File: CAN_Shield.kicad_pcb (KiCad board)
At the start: 2 copper layers, 65 x 56 mm, 5 parts, among them J1 GPIO

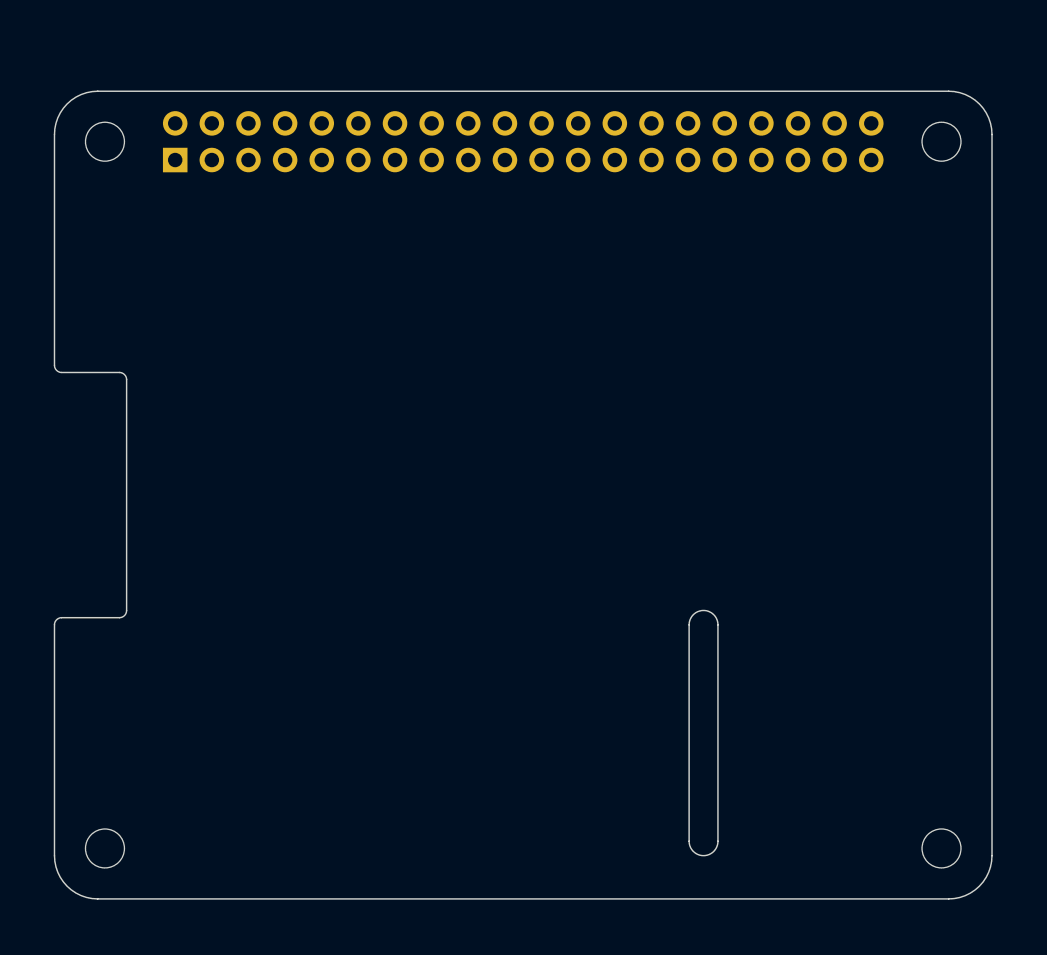
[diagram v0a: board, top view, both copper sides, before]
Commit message: finished layout with 9 pin screw terminal, Unfinished edge extend and diff pair CAN
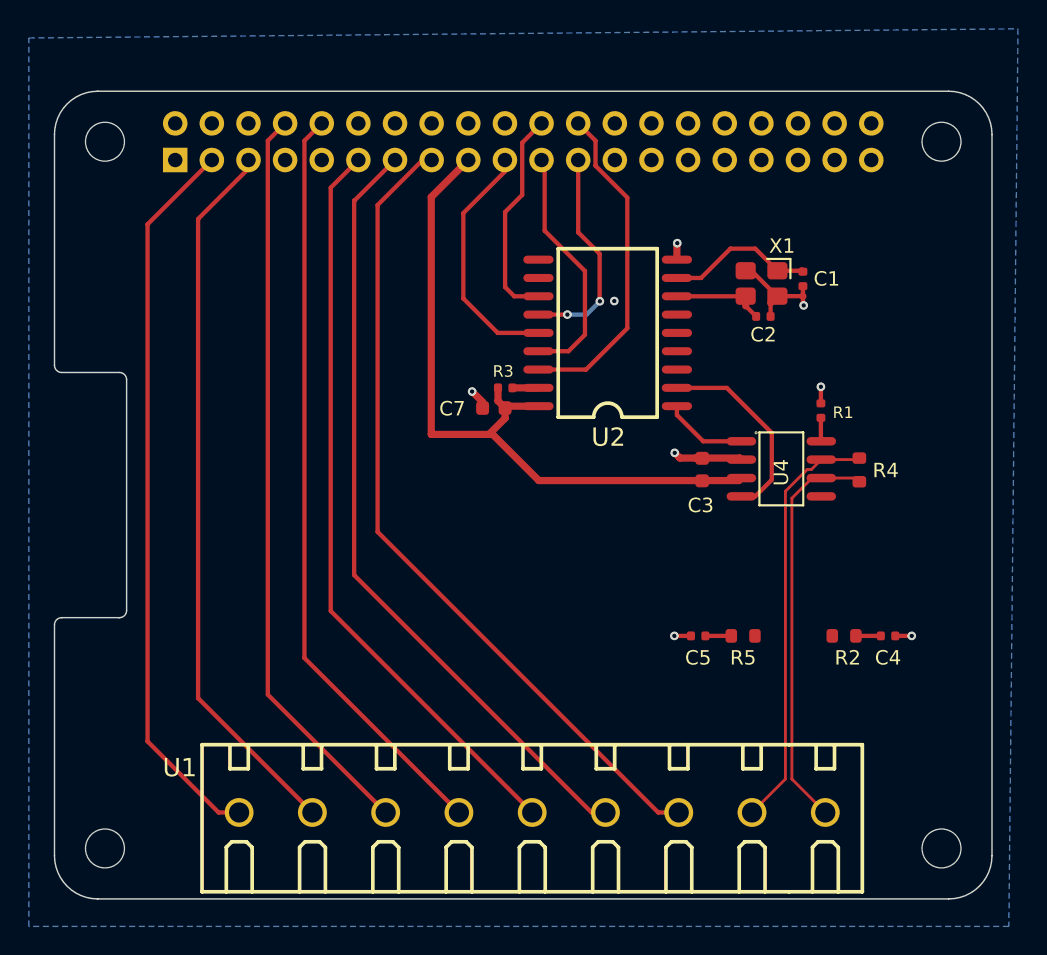
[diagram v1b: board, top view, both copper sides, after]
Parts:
- added C1: 22pF, PCM_JLCPCB:C_0402, F.Cu at (151.9, 57.0)
- added C2: 22pF, PCM_JLCPCB:C_0402, F.Cu at (149.1, 59.6)
- added C3: 100nF, PCM_JLCPCB:C_0603, F.Cu at (144.9, 70.2)
- added C4: 470pF, PCM_JLCPCB:C_0402, F.Cu at (157.8, 81.8)
- added C5: 470pF, PCM_JLCPCB:C_0402, F.Cu at (144.6, 81.8)
- added C7: 100nF, PCM_JLCPCB:C_0603, F.Cu at (130.5, 66.0)
- added R1: 4.7kΩ, PCM_JLCPCB:R_0402, F.Cu at (153.1, 66.1)
- added R2: 120Ω, PCM_JLCPCB:R_0603, F.Cu at (154.7, 81.8)
- added R3: 4.7kΩ, PCM_JLCPCB:R_0402, F.Cu at (131.2, 64.6)
- added R4: 120Ω, PCM_JLCPCB:R_0603, F.Cu at (155.8, 70.3)
- added R5: 120Ω, PCM_JLCPCB:R_0603, F.Cu at (147.7, 81.8)
- added U1: MX128-5.08-09P-GN01-CU-Y-A, ImportFP:CONN-TH_9P-P5.08_MX128-5.08-09P-GN01-CU-Y-A, F.Cu at (133.1, 94.0)
- added U2: MCP2515T-I/SO, ImportFP:MCP2515T-IST_SOIC-18_L11.6-W7.5-P1.27-LS10.3-BL, F.Cu at (138.4, 60.8)
- added U4: SN65HVD230DR, PCM_JLCPCB:SOIC-8_L4.9-W3.9-P1.27-LS6.0-BL, F.Cu at (150.4, 70.2)
- added X1: X322516MLB4SI, PCM_JLCPCB:OSC-SMD_4P-L3.2-W2.5-BL, F.Cu at (149.0, 57.3)
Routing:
- net /GPIO22: track 0.00 -> 56.6 mm
- net /GPIO27: track 0.00 -> 54.2 mm
- net /GPIO15/RXD0: track 0.00 -> 52.7 mm
- net /GPIO17: track 0.00 -> 51.8 mm
- net /GPIO14/TXD0: track 0.00 -> 51.7 mm
- net /GPIO2/SDA1: track 0.00 -> 50.5 mm
- net /GPIO3/SCL1: track 0.00 -> 50.0 mm
- net +3V3: track 0.00 -> 49.2 mm
- net /CAN_D+: track 0.00 -> 29.3 mm
- net /CAN_D-: track 0.00 -> 28.1 mm
- net /GPIO8/SPI0.CE0: track 0.00 -> 23.0 mm
- net GND: track 0.00 -> 19.3 mm, vias 0 -> 8
- net /GPIO9/SPI0.MISO: track 0.00 -> 17.1 mm
- net /GPIO10/SPI0.MOSI: track 0.00 -> 17.0 mm
- net /GPIO11/SPI0.SCLK: track 0.00 -> 15.1 mm, vias 0 -> 2
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- added copper zone on B.Cu, net GND
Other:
- outline, holes or cut-outs redrawn
- board text removed: "CAMERA (OPTIONAL)"

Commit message: change from gpio to gnd at screw terminal and add copper pour for gnd
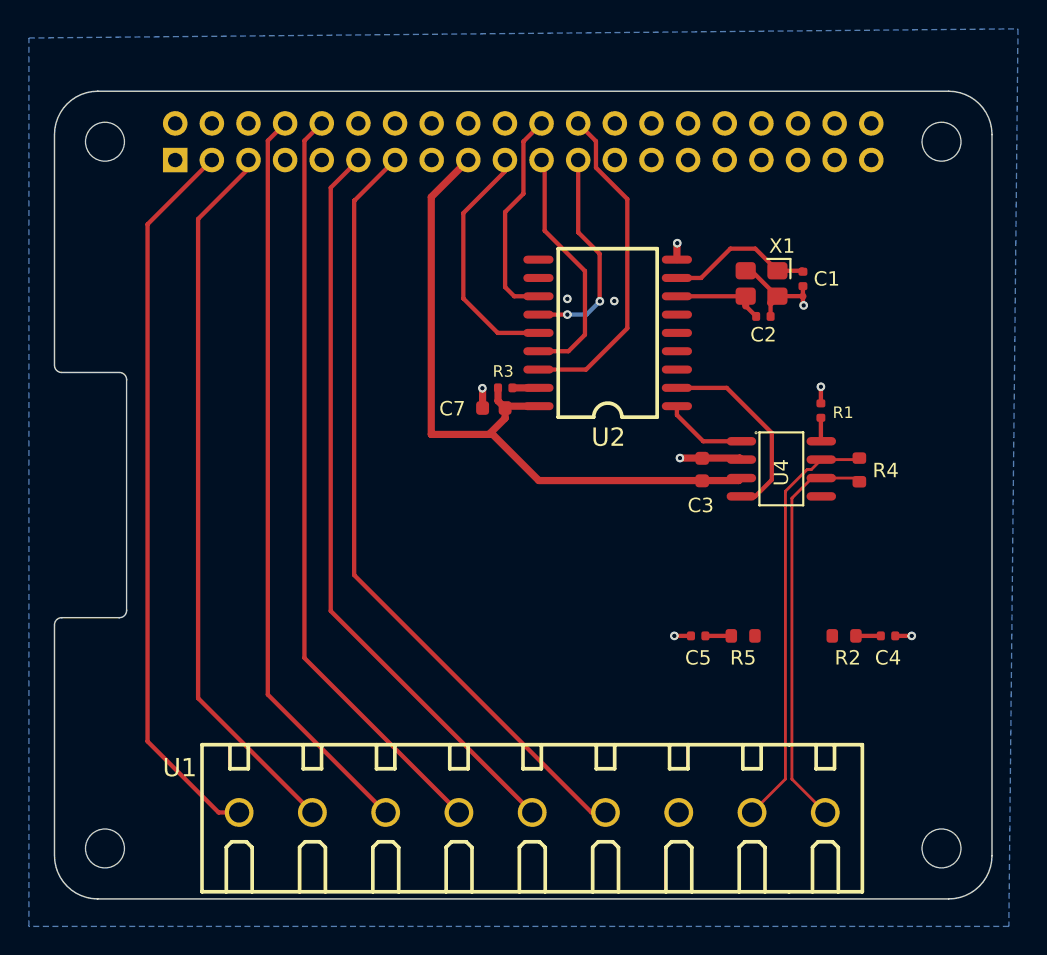
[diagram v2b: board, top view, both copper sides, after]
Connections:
- U1 pad 7: /GPIO22 -> GND
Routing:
- net /GPIO22: track 56.6 -> 0.62 mm
- net GND: track 19.3 -> 18.7 mm, vias 8 -> 9
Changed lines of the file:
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@@
 			)
 			(remove_unused_layers no)
-			(net 10 "/GPIO22")
+			(net 1 "GND")
 			(pinfunction "7")
 			(pintype "unspecified")
@@
 			(net 10 "/GPIO22")
 			(pinfunction "Pin_15")
-			(pintype "passive")
+			(pintype "passive+no_connect")
 		)
 		(pad "16" thru_hole oval
@@
 	)
 	(segment
-		(start 147.5164 69.4332)
-		(end 147.6236 69.5404)
-		(width 0.5)
-		(layer "F.Cu")
-		(net 1)
-	)
-	(segment
 		(start 149.649 59.614)
 		(end 149.649 58.681)
@@
 	)
 	(segment
+		(start 147.5164 69.4332)
+		(end 147.6236 69.5404)
+		(width 0.5)
+		(layer "F.Cu")
+		(net 1)
+	)
+	(segment
 		(start 148.325122 56.448)
 		(end 150.085122 58.208)
@@
 	)
 	(segment
-		(start 144.45 69.4332)
-		(end 147.5164 69.4332)
-		(width 0.5)
-		(layer "F.Cu")
-		(net 1)
-	)
-	(segment
 		(start 158.293 81.7628)
 		(end 159.436 81.7628)
@@
 	)
 	(segment
-		(start 129.682 65.964)
-		(end 129.682 65.547)
+		(start 149.649 58.681)
+		(end 150.122 58.208)
 		(width 0.5)
 		(layer "F.Cu")
@@
 	)
 	(segment
-		(start 149.649 58.681)
-		(end 150.122 58.208)
+		(start 151.891 58.8)
+		(end 151.943 58.852)
 		(width 0.5)
 		(layer "F.Cu")
@@
 	)
 	(segment
-		(start 151.891 58.8)
-		(end 151.943 58.852)
+		(start 129.682 64.6072)
+		(end 129.682 65.964)
 		(width 0.5)
 		(layer "F.Cu")
@@
 	)
 	(segment
-		(start 129.682 65.547)
-		(end 128.956 64.821)
+		(start 143.3652 69.4332)
+		(end 147.5164 69.4332)
 		(width 0.5)
 		(layer "F.Cu")
@@
 	)
 	(segment
-		(start 143.3652 69.4332)
-		(end 143.0022 69.0702)
+		(start 129.6672 64.5924)
+		(end 129.682 64.6072)
 		(width 0.5)
 		(layer "F.Cu")
@@
 	)
 	(segment
-		(start 144.45 69.4332)
-		(end 143.3652 69.4332)
-		(width 0.5)
-		(layer "F.Cu")
-		(net 1)
-	)
-	(segment
 		(start 143.1541 54.5599)
 		(end 143.18 54.534)
@@
 	)
 	(via
+		(at 135.56 58.3948)
+		(size 0.6)
+		(drill 0.3)
+		(layers "F.Cu" "B.Cu")
+		(net 1)
+	)
+	(via
 		(at 142.9768 81.7628)
 		(size 0.6)
@@
 	)
 	(via
-		(at 128.956 64.821)
+		(at 129.6672 64.5924)
 		(size 0.6)
 		(drill 0.3)
@@
 	)
 	(via
-		(at 143.0022 69.0702)
+		(at 143.3652 69.4332)
 		(size 0.6)
 		(drill 0.3)
@@
 	)
 	(segment
-		(start 122.4028 74.5492)
-		(end 141.8592 94.0056)
-		(width 0.3)
-		(layer "F.Cu")
-		(net 10)
-	)
-	(segment
-		(start 125.5252 48.77)
-		(end 122.4028 51.8924)
-		(width 0.3)
-		(layer "F.Cu")
-		(net 10)
-	)
-	(segment
 		(start 126.15 48.77)
 		(end 125.5252 48.77)
@@
 	)
 	(segment
-		(start 122.4028 51.8924)
-		(end 122.4028 74.5492)
-		(width 0.3)
-		(layer "F.Cu")
-		(net 10)
-	)
-	(segment
-		(start 141.8592 94.0056)
-		(end 143.2816 94.0056)
-		(width 0.3)
-		(layer "F.Cu")
-		(net 10)
-	)
-	(segment
 		(start 128.3464 52.4512)
 		(end 128.3464 58.3694)
@@
 	)
 	(segment
-		(start 131.242 57.582)
-		(end 131.877 58.217)
+		(start 131.877 58.217)
+		(end 133.5539 58.217)
 		(width 0.3)
 		(layer "F.Cu")
@@
 	)
 	(segment
-		(start 131.242 52.375)
-		(end 131.242 57.582)
+		(start 132.512 51.105)
+		(end 131.242 52.375)
 		(width 0.3)
 		(layer "F.Cu")
@@
 	)
 	(segment
-		(start 132.43 47.57)
-		(end 132.43 51.187)
+		(start 131.242 57.582)
+		(end 131.877 58.217)
 		(width 0.3)
 		(layer "F.Cu")
@@
 	)
 	(segment
-		(start 133.77 46.23)
-		(end 132.43 47.57)
+		(start 132.512 47.488)
+		(end 132.512 51.105)
 		(width 0.3)
 		(layer "F.Cu")
@@
 	)
 	(segment
-		(start 131.877 58.217)
-		(end 133.5539 58.217)
+		(start 131.242 52.375)
+		(end 131.242 57.582)
 		(width 0.3)
 		(layer "F.Cu")
@@
 	)
 	(segment
-		(start 132.43 51.187)
-		(end 131.242 52.375)
+		(start 133.77 46.23)
+		(end 132.512 47.488)
 		(width 0.3)
 		(layer "F.Cu")
@@
 	)
 	(segment
-		(start 136.8554 63.297)
-		(end 133.5539 63.297)
+		(start 137.5412 47.4612)
+		(end 137.5412 49.3016)
 		(width 0.3)
 		(layer "F.Cu")
@@
 	)
 	(segment
-		(start 137.51 47.43)
-		(end 137.51 49.1688)
+		(start 139.7152 51.4756)
+		(end 139.7152 60.4372)
 		(width 0.3)
 		(layer "F.Cu")
@@
 	)
 	(segment
-		(start 137.51 49.1688)
-		(end 139.7152 51.374)
+		(start 136.8554 63.297)
+		(end 133.5539 63.297)
 		(width 0.3)
 		(layer "F.Cu")
@@
 	)
 	(segment
-		(start 139.7152 51.374)
-		(end 139.7152 60.4372)
+		(start 137.5412 49.3016)
+		(end 139.7152 51.4756)
 		(width 0.3)
 		(layer "F.Cu")
@@
 	(segment
 		(start 136.31 46.23)
-		(end 137.51 47.43)
+		(end 137.5412 47.4612)
 		(width 0.3)
 		(layer "F.Cu")

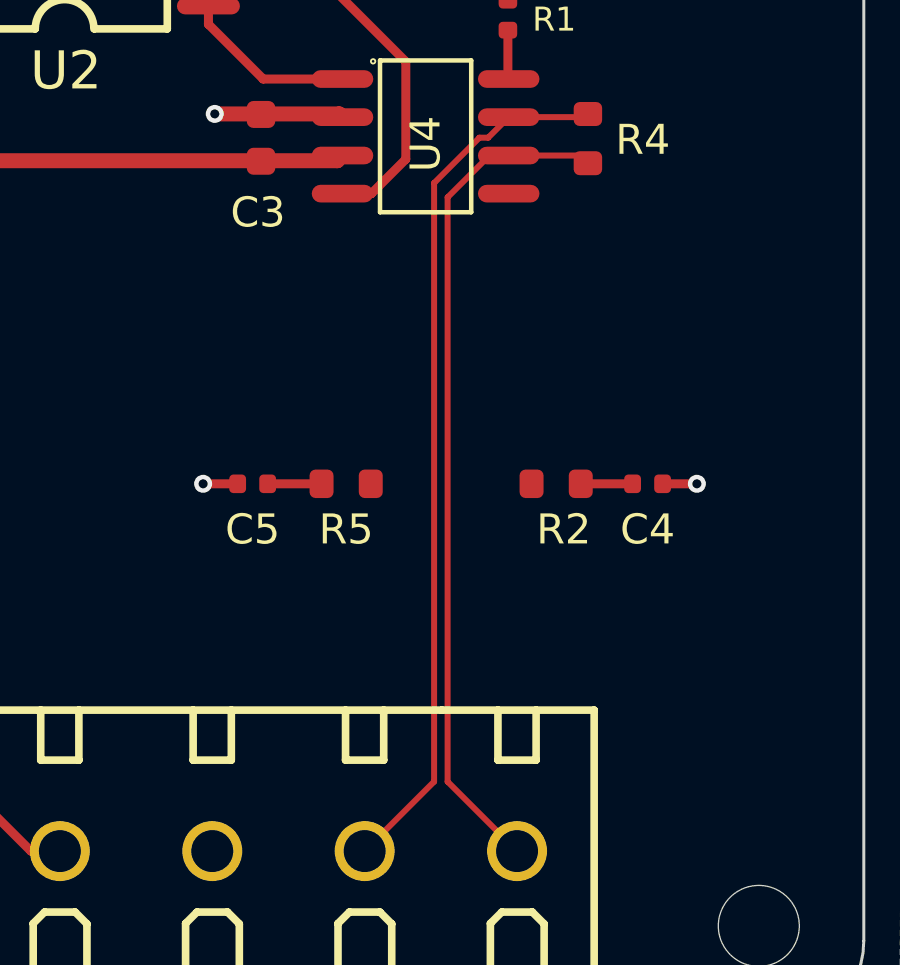
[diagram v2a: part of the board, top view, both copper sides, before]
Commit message: add R and C to CAN H,L diff pair
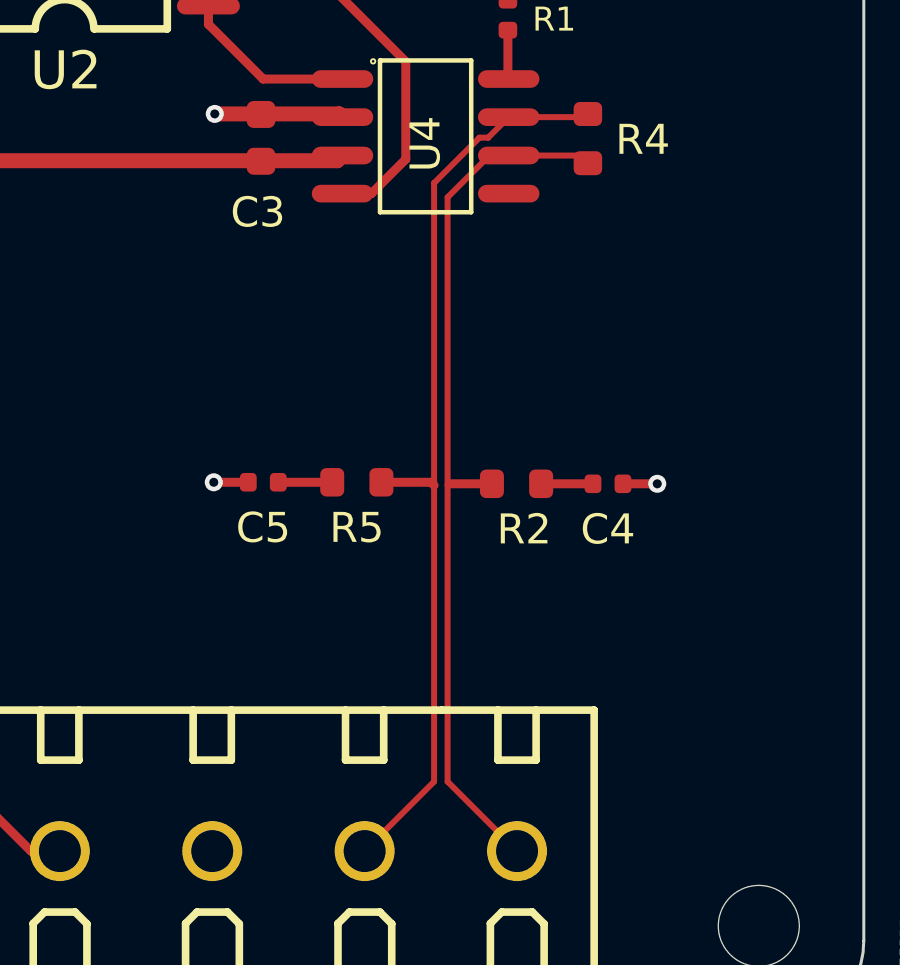
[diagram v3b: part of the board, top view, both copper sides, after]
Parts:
- moved C4 1.32 mm to (156.5, 81.8)
- moved R2 1.32 mm to (153.4, 81.8)
- moved R5 0.36 mm to (148.1, 81.7)
- moved C5 0.36 mm to (145.0, 81.7)
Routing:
- net /CAN_D+: track 29.3 -> 31.1 mm
- net /CAN_D-: track 28.1 -> 29.5 mm
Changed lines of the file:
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@@
 	(footprint "PCM_JLCPCB:C_0402"
 		(layer "F.Cu")
-		(at 144.6278 81.7628 180)
+		(at 144.9834 81.712 180)
 		(descr "Capacitor SMD 0402 (1005 Metric), square (rectangular) end terminal, IPC_7351 nominal, (Body size source: IPC-SM-782 page 76, https://www.pcb-3d.com/wordpress/wp-content/uploads/ipc-sm-782a_amendment_1_and_2.pdf), generated with kicad-footprint-generator")
 		(tags "capacitor")
@@
 	(footprint "PCM_JLCPCB:R_0603"
 		(layer "F.Cu")
-		(at 147.7448 81.7628 180)
+		(at 148.1004 81.712 180)
 		(descr "Resistor SMD 0603 (1608 Metric), square (rectangular) end terminal, IPC_7351 nominal, (Body size source: IPC-SM-782 page 72, https://www.pcb-3d.com/wordpress/wp-content/uploads/ipc-sm-782a_amendment_1_and_2.pdf), generated with kicad-footprint-generator")
 		(tags "resistor")
@@
 	(footprint "PCM_JLCPCB:C_0402"
 		(layer "F.Cu")
-		(at 157.793 81.7628)
+		(at 156.4722 81.7628)
 		(descr "Capacitor SMD 0402 (1005 Metric), square (rectangular) end terminal, IPC_7351 nominal, (Body size source: IPC-SM-782 page 76, https://www.pcb-3d.com/wordpress/wp-content/uploads/ipc-sm-782a_amendment_1_and_2.pdf), generated with kicad-footprint-generator")
 		(tags "capacitor")
@@
 	(footprint "PCM_JLCPCB:R_0603"
 		(layer "F.Cu")
-		(at 154.745 81.7628)
+		(at 153.4242 81.7628)
 		(descr "Resistor SMD 0603 (1608 Metric), square (rectangular) end terminal, IPC_7351 nominal, (Body size source: IPC-SM-782 page 72, https://www.pcb-3d.com/wordpress/wp-content/uploads/ipc-sm-782a_amendment_1_and_2.pdf), generated with kicad-footprint-generator")
 		(tags "resistor")
@@
 	)
 	(segment
-		(start 144.1278 81.7628)
-		(end 142.9768 81.7628)
+		(start 144.4834 81.712)
+		(end 143.3324 81.712)
 		(width 0.3)
 		(layer "F.Cu")
@@
 	)
 	(segment
-		(start 158.293 81.7628)
-		(end 159.436 81.7628)
+		(start 156.9722 81.7628)
+		(end 158.1152 81.7628)
 		(width 0.3)
 		(layer "F.Cu")
@@
 	)
 	(via
-		(at 142.9768 81.7628)
+		(at 143.3324 81.712)
 		(size 0.6)
 		(drill 0.3)
@@
 	)
 	(via
-		(at 159.436 81.7628)
+		(at 158.1152 81.7628)
 		(size 0.6)
 		(drill 0.3)
@@
 	)
 	(segment
-		(start 145.1278 81.7628)
-		(end 146.9248 81.7628)
+		(start 145.4834 81.712)
+		(end 147.2804 81.712)
 		(width 0.3)
 		(layer "F.Cu")
@@
 	)
 	(segment
-		(start 155.565 81.7628)
-		(end 157.293 81.7628)
+		(start 154.2442 81.7628)
+		(end 155.9722 81.7628)
 		(width 0.3)
 		(layer "F.Cu")
@@
 	)
 	(segment
+		(start 152.6042 81.7628)
+		(end 151.177401 81.7628)
+		(width 0.3)
+		(layer "F.Cu")
+		(net 47)
+	)
+	(segment
 		(start 151.126601 91.690601)
 		(end 153.4416 94.0056)
@@
 	)
 	(segment
+		(start 151.126601 72.213796)
+		(end 151.126601 81.8136)
+		(width 0.2)
+		(layer "F.Cu")
+		(net 47)
+	)
+	(segment
 		(start 153.1636 70.8204)
 		(end 155.5478 70.8204)
@@
 	)
 	(segment
-		(start 151.126601 72.213796)
+		(start 151.126601 81.8136)
 		(end 151.126601 91.690601)
 		(width 0.2)
@@
 	)
 	(segment
-		(start 148.5648 81.7628)
-		(end 148.5902 81.7374)
+		(start 150.574999 81.712)
+		(end 150.676599 81.8136)
 		(width 0.3)
 		(layer "F.Cu")
@@
 	)
 	(segment
-		(start 150.676599 71.735944)
+		(start 148.9204 81.712)
+		(end 150.574999 81.712)
+		(width 0.3)
+		(layer "F.Cu")
+		(net 48)
+	)
+	(segment
+		(start 150.676599 81.8136)
 		(end 150.676599 91.690601)
 		(width 0.2)
@@
 	)
 	(segment
+		(start 148.9204 81.712)
+		(end 148.9458 81.6866)
+		(width 0.3)
+		(layer "F.Cu")
+		(net 48)
+	)
+	(segment
 		(start 152.4786 70.2254)
 		(end 152.187143 70.2254)
@@
 		(width 0.2)
 		(layer "F.Cu")
+		(net 48)
+	)
+	(segment
+		(start 150.676599 71.735944)
+		(end 150.676599 81.8136)
+		(width 0.2)
+		(layer "F.Cu")
